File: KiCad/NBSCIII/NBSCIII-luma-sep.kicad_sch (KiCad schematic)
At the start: 11 parts, among them U1 LM324N

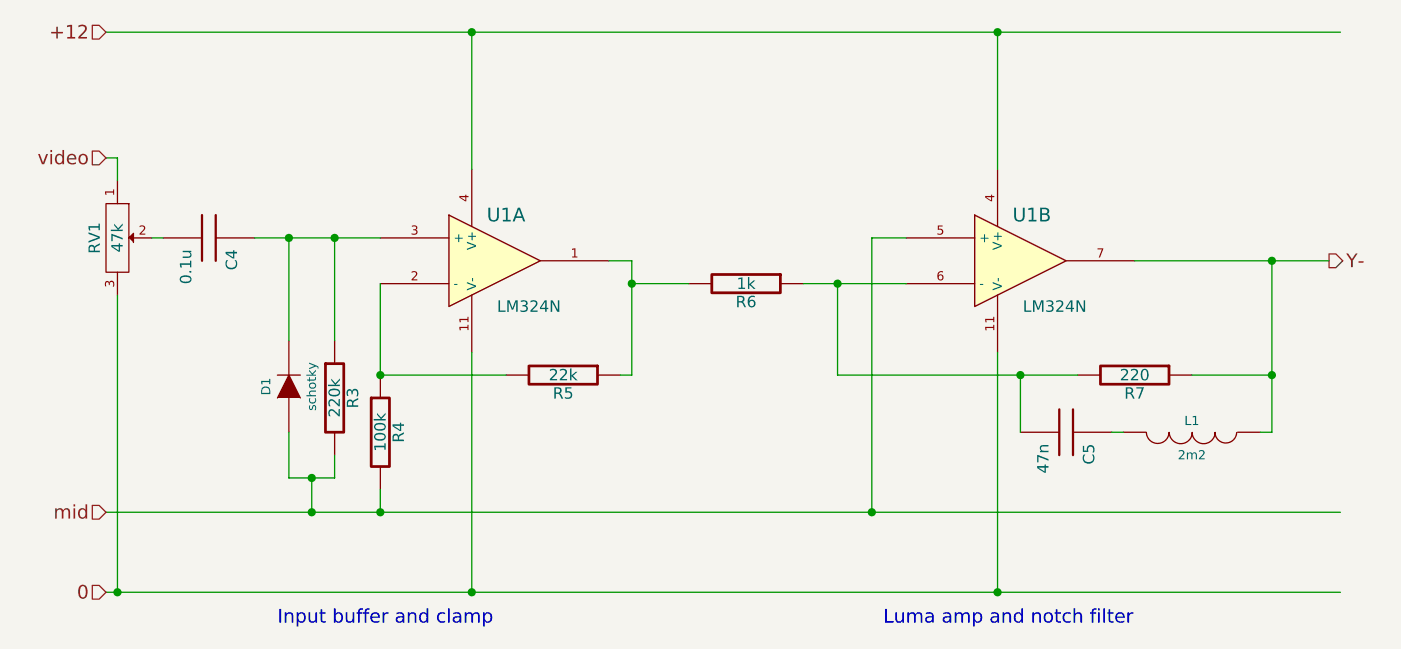
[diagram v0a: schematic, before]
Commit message: unrescue to Device:C
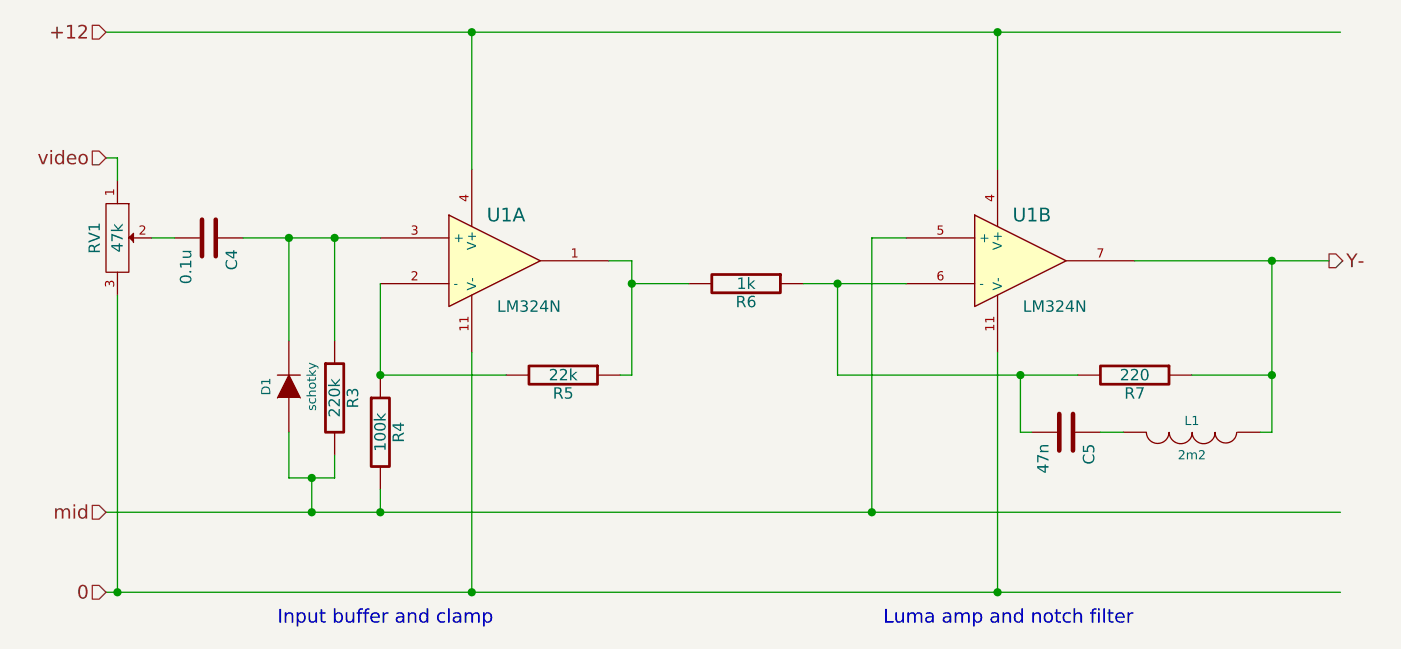
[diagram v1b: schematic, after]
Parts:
- C4, C5: symbol NBSCIII-rescue:C -> Device:C
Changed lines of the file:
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@@
     (stroke (width 0) (type default) (color 0 0 0 0))
   )
-  (wire (pts (xy 48.26 59.69) (xy 49.53 59.69))
+  (wire (pts (xy 48.26 59.69) (xy 50.8 59.69))
     (stroke (width 0) (type default) (color 0 0 0 0))
   )
@@
     (stroke (width 0) (type default) (color 0 0 0 0))
   )
-  (wire (pts (xy 154.94 81.28) (xy 156.21 81.28))
-    (stroke (width 0) (type default) (color 0 0 0 0))
-  )
   (wire (pts (xy 101.6 64.77) (xy 101.6 74.93))
     (stroke (width 0) (type default) (color 0 0 0 0))
@@
     (stroke (width 0) (type default) (color 0 0 0 0))
   )
-  (wire (pts (xy 59.69 59.69) (xy 63.5 59.69))
+  (wire (pts (xy 58.42 59.69) (xy 63.5 59.69))
     (stroke (width 0) (type default) (color 0 0 0 0))
   )
@@
     (stroke (width 0) (type default) (color 0 0 0 0))
   )
+  (wire (pts (xy 144.78 81.28) (xy 146.05 81.28))
+    (stroke (width 0) (type default) (color 0 0 0 0))
+  )
   (wire (pts (xy 66.04 86.36) (xy 63.5 86.36))
     (stroke (width 0) (type default) (color 0 0 0 0))
@@
   )
   (wire (pts (xy 68.58 86.36) (xy 66.04 86.36))
+    (stroke (width 0) (type default) (color 0 0 0 0))
+  )
+  (wire (pts (xy 153.67 81.28) (xy 156.21 81.28))
     (stroke (width 0) (type default) (color 0 0 0 0))
   )
@@
     (pin "3")
   )
-  (symbol (lib_id "NBSCIII-rescue:C") (at 54.61 59.69 270) (unit 1)
+  (symbol (lib_id "Device:C") (at 54.61 59.69 270) (unit 1)
     (in_bom yes) (on_board yes)
     (property "Reference" "C4" (id 0) (at 57.15 60.96 0)
@@
     (pin "2")
   )
-  (symbol (lib_id "NBSCIII-rescue:C") (at 149.86 81.28 270) (unit 1)
+  (symbol (lib_id "Device:C") (at 149.86 81.28 270) (unit 1)
     (in_bom yes) (on_board yes)
     (property "Reference" "C5" (id 0) (at 152.4 82.55 0)

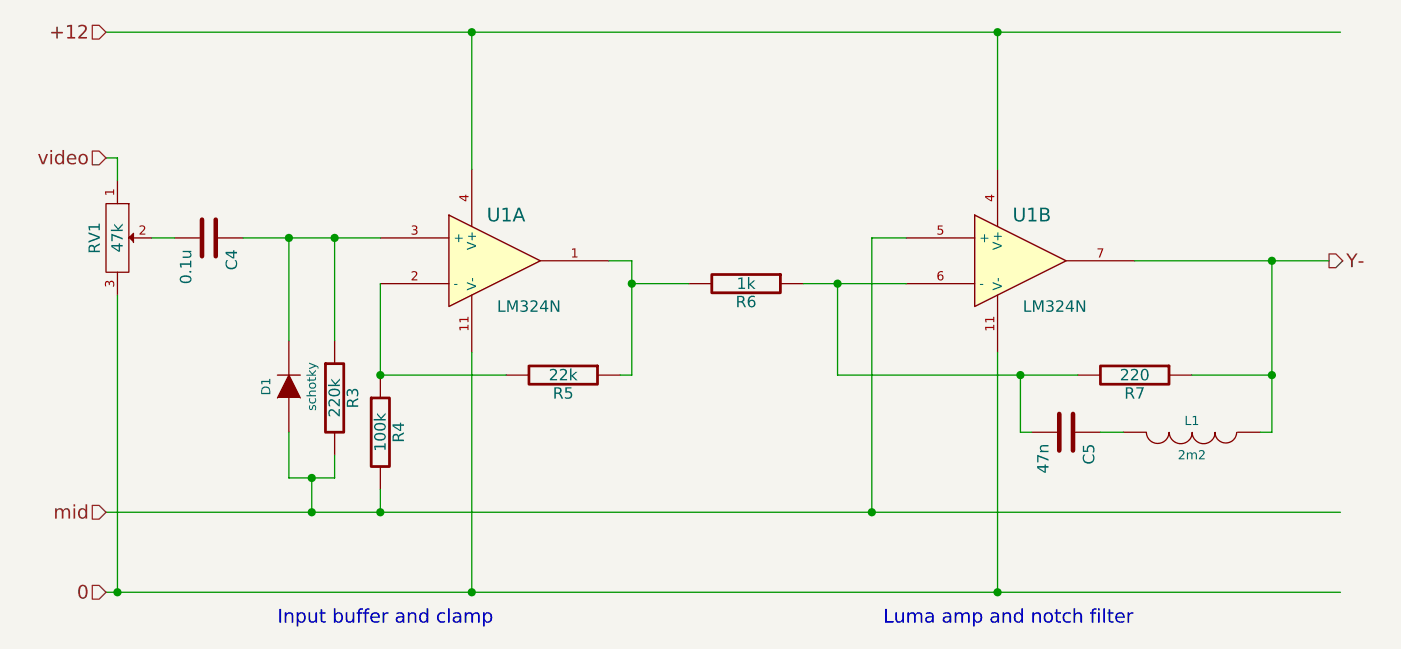
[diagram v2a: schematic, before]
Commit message: unrescue Device:R
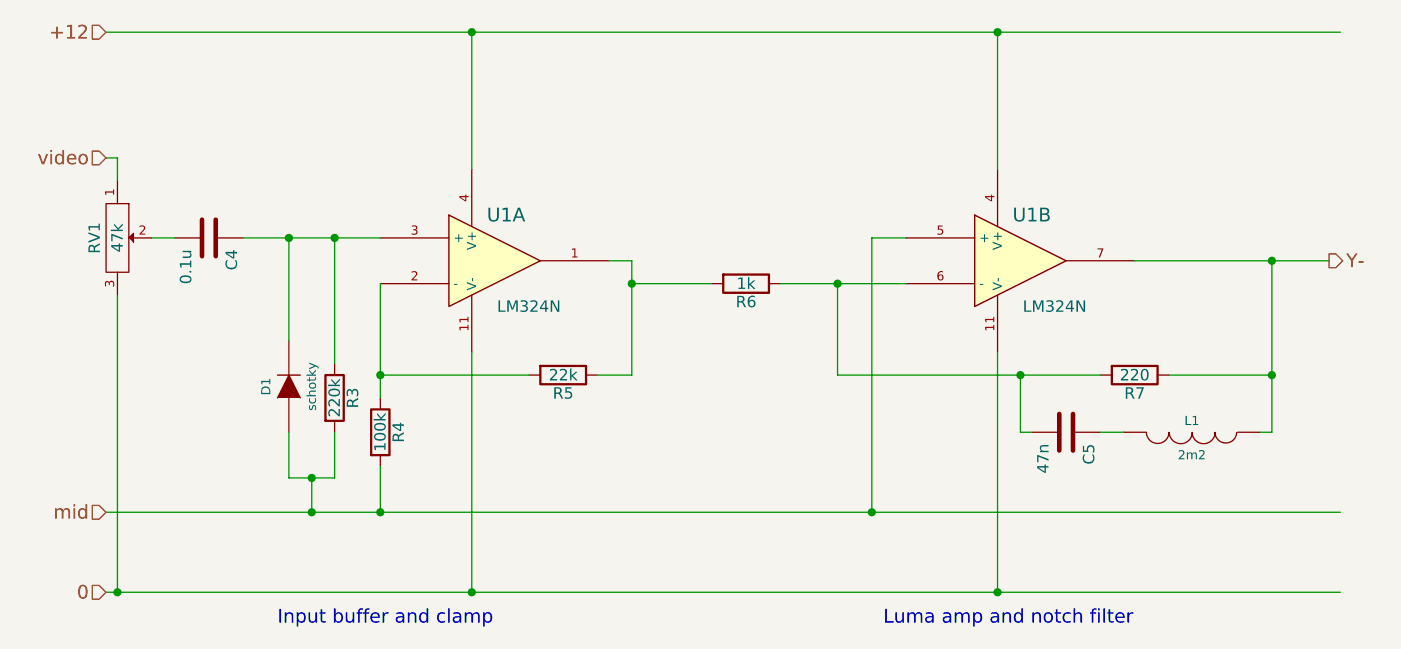
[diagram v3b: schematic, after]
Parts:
- R3, R4, R5, R6, R7: symbol NBSCIII-rescue:R -> Device:R
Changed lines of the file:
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@@
   (junction (at 73.66 90.17) (diameter 0) (color 0 0 0 0)
   )
+  (junction (at 73.66 74.93) (diameter 0) (color 0 0 0 0)
+  )
   (junction (at 172.72 74.93) (diameter 0) (color 0 0 0 0)
   )
@@
   (junction (at 101.6 64.77) (diameter 0) (color 0 0 0 0)
   )
-  (junction (at 73.66 74.93) (diameter 0) (color 0 0 0 0)
-  )
   (junction (at 66.04 86.36) (diameter 0) (color 0 0 0 0)
   )
@@
     (stroke (width 0) (type default) (color 0 0 0 0))
   )
-  (wire (pts (xy 73.66 90.17) (xy 73.66 87.63))
-    (stroke (width 0) (type default) (color 0 0 0 0))
-  )
-  (wire (pts (xy 68.58 59.69) (xy 68.58 71.12))
+  (wire (pts (xy 73.66 85.09) (xy 73.66 90.17))
     (stroke (width 0) (type default) (color 0 0 0 0))
   )
@@
     (stroke (width 0) (type default) (color 0 0 0 0))
   )
+  (wire (pts (xy 68.58 59.69) (xy 68.58 73.66))
+    (stroke (width 0) (type default) (color 0 0 0 0))
+  )
   (wire (pts (xy 73.66 64.77) (xy 73.66 74.93))
     (stroke (width 0) (type default) (color 0 0 0 0))
   )
-  (wire (pts (xy 101.6 64.77) (xy 107.95 64.77))
+  (wire (pts (xy 101.6 64.77) (xy 110.49 64.77))
     (stroke (width 0) (type default) (color 0 0 0 0))
   )
@@
     (stroke (width 0) (type default) (color 0 0 0 0))
   )
+  (wire (pts (xy 73.66 74.93) (xy 73.66 77.47))
+    (stroke (width 0) (type default) (color 0 0 0 0))
+  )
   (wire (pts (xy 63.5 71.12) (xy 63.5 59.69))
     (stroke (width 0) (type default) (color 0 0 0 0))
   )
-  (wire (pts (xy 124.46 64.77) (xy 120.65 64.77))
+  (wire (pts (xy 118.11 64.77) (xy 124.46 64.77))
     (stroke (width 0) (type default) (color 0 0 0 0))
   )
@@
     (stroke (width 0) (type default) (color 0 0 0 0))
   )
-  (wire (pts (xy 73.66 74.93) (xy 87.63 74.93))
+  (wire (pts (xy 73.66 74.93) (xy 90.17 74.93))
     (stroke (width 0) (type default) (color 0 0 0 0))
   )
@@
     (stroke (width 0) (type default) (color 0 0 0 0))
   )
-  (wire (pts (xy 151.13 74.93) (xy 144.78 74.93))
+  (wire (pts (xy 144.78 74.93) (xy 153.67 74.93))
     (stroke (width 0) (type default) (color 0 0 0 0))
   )
@@
     (stroke (width 0) (type default) (color 0 0 0 0))
   )
-  (wire (pts (xy 172.72 74.93) (xy 163.83 74.93))
+  (wire (pts (xy 161.29 74.93) (xy 172.72 74.93))
     (stroke (width 0) (type default) (color 0 0 0 0))
   )
@@
     (stroke (width 0) (type default) (color 0 0 0 0))
   )
-  (wire (pts (xy 68.58 83.82) (xy 68.58 86.36))
+  (wire (pts (xy 68.58 81.28) (xy 68.58 86.36))
     (stroke (width 0) (type default) (color 0 0 0 0))
   )
@@
     (stroke (width 0) (type default) (color 0 0 0 0))
   )
-  (wire (pts (xy 101.6 74.93) (xy 100.33 74.93))
+  (wire (pts (xy 97.79 74.93) (xy 101.6 74.93))
     (stroke (width 0) (type default) (color 0 0 0 0))
   )
@@
     (pin "2")
   )
-  (symbol (lib_id "NBSCIII-rescue:R") (at 68.58 77.47 0) (unit 1)
+  (symbol (lib_id "Device:R") (at 68.58 77.47 0) (unit 1)
     (in_bom yes) (on_board yes)
     (property "Reference" "R3" (id 0) (at 70.612 77.47 90))
@@
     (pin "2")
   )
-  (symbol (lib_id "NBSCIII-rescue:R") (at 73.66 81.28 0) (unit 1)
+  (symbol (lib_id "Device:R") (at 73.66 81.28 0) (unit 1)
     (in_bom yes) (on_board yes)
     (property "Reference" "R4" (id 0) (at 75.692 81.28 90))
@@
     (pin "2")
   )
-  (symbol (lib_id "NBSCIII-rescue:R") (at 93.98 74.93 270) (unit 1)
+  (symbol (lib_id "Device:R") (at 93.98 74.93 270) (unit 1)
     (in_bom yes) (on_board yes)
     (property "Reference" "R5" (id 0) (at 93.98 76.962 90))
@@
     (pin "14")
   )
-  (symbol (lib_id "NBSCIII-rescue:R") (at 114.3 64.77 270) (unit 1)
+  (symbol (lib_id "Device:R") (at 114.3 64.77 270) (unit 1)
     (in_bom yes) (on_board yes)
     (property "Reference" "R6" (id 0) (at 114.3 66.802 90))
@@
     (pin "2")
   )
-  (symbol (lib_id "NBSCIII-rescue:R") (at 157.48 74.93 270) (unit 1)
+  (symbol (lib_id "Device:R") (at 157.48 74.93 270) (unit 1)
     (in_bom yes) (on_board yes)
     (property "Reference" "R7" (id 0) (at 157.48 76.962 90))

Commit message: unrescue Device:R_potentiometer
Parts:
- RV1: symbol NBSCIII-rescue:POT -> Device:R_Potentiometer
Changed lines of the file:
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@@
     (stroke (width 0) (type default) (color 0 0 0 0))
   )
-  (wire (pts (xy 44.45 99.06) (xy 44.45 66.04))
+  (wire (pts (xy 44.45 63.5) (xy 44.45 99.06))
     (stroke (width 0) (type default) (color 0 0 0 0))
   )
@@
   )
   (wire (pts (xy 83.82 52.07) (xy 83.82 36.83))
+    (stroke (width 0) (type default) (color 0 0 0 0))
+  )
+  (wire (pts (xy 44.45 50.8) (xy 44.45 55.88))
     (stroke (width 0) (type default) (color 0 0 0 0))
   )
@@
   )
   (wire (pts (xy 172.72 62.23) (xy 179.07 62.23))
-    (stroke (width 0) (type default) (color 0 0 0 0))
-  )
-  (wire (pts (xy 44.45 53.34) (xy 44.45 50.8))
     (stroke (width 0) (type default) (color 0 0 0 0))
   )
@@
     (pin "14")
   )
-  (symbol (lib_id "NBSCIII-rescue:POT") (at 44.45 59.69 270) (unit 1)
+  (symbol (lib_id "Device:R_Potentiometer") (at 44.45 59.69 0) (unit 1)
     (in_bom yes) (on_board yes)
-    (property "Reference" "RV1" (id 0) (at 41.91 59.69 0))
-    (property "Value" "47k" (id 1) (at 44.45 59.69 0))
+    (property "Reference" "RV1" (id 0) (at 39.37 63.5 0))
+    (property "Value" "47k" (id 1) (at 44.45 59.69 90))
     (property "Footprint" "" (id 2) (at 44.45 59.69 0)
       (effects (font (size 1.27 1.27)) hide)

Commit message: unrescue Device:D
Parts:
- D1: symbol NBSCIII-rescue:DIODE -> Device:D
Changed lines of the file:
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@@
     (stroke (width 0) (type default) (color 0 0 0 0))
   )
-  (wire (pts (xy 63.5 71.12) (xy 63.5 59.69))
+  (wire (pts (xy 63.5 59.69) (xy 63.5 72.39))
     (stroke (width 0) (type default) (color 0 0 0 0))
   )
@@
     (stroke (width 0) (type default) (color 0 0 0 0))
   )
-  (wire (pts (xy 63.5 86.36) (xy 63.5 81.28))
+  (wire (pts (xy 63.5 80.01) (xy 63.5 86.36))
     (stroke (width 0) (type default) (color 0 0 0 0))
   )
@@
     (pin "2")
   )
-  (symbol (lib_id "NBSCIII-rescue:DIODE") (at 63.5 76.2 90) (unit 1)
+  (symbol (lib_id "Device:D") (at 63.5 76.2 90) (unit 1)
     (in_bom yes) (on_board yes)
     (property "Reference" "D1" (id 0) (at 60.96 76.2 0)

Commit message: unrescue Device:L_small
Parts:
- L1: symbol NBSCIII-rescue:INDUCTOR -> Device:L_Small
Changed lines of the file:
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@@
     (stroke (width 0) (type default) (color 0 0 0 0))
   )
-  (wire (pts (xy 153.67 81.28) (xy 156.21 81.28))
+  (wire (pts (xy 153.67 81.28) (xy 161.29 81.28))
     (stroke (width 0) (type default) (color 0 0 0 0))
   )
@@
     (stroke (width 0) (type default) (color 0 0 0 0))
   )
-  (wire (pts (xy 171.45 81.28) (xy 172.72 81.28))
+  (wire (pts (xy 166.37 81.28) (xy 172.72 81.28))
     (stroke (width 0) (type default) (color 0 0 0 0))
   )
@@
     (pin "2")
   )
-  (symbol (lib_id "NBSCIII-rescue:INDUCTOR") (at 163.83 81.28 270) (unit 1)
+  (symbol (lib_id "Device:L_Small") (at 163.83 81.28 270) (unit 1)
     (in_bom yes) (on_board yes)
     (property "Reference" "L1" (id 0) (at 163.83 80.01 90)

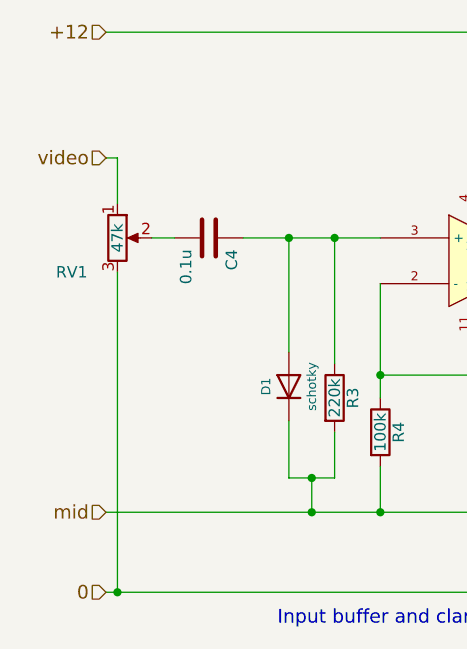
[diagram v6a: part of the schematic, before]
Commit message: Simplify power distribution and make global
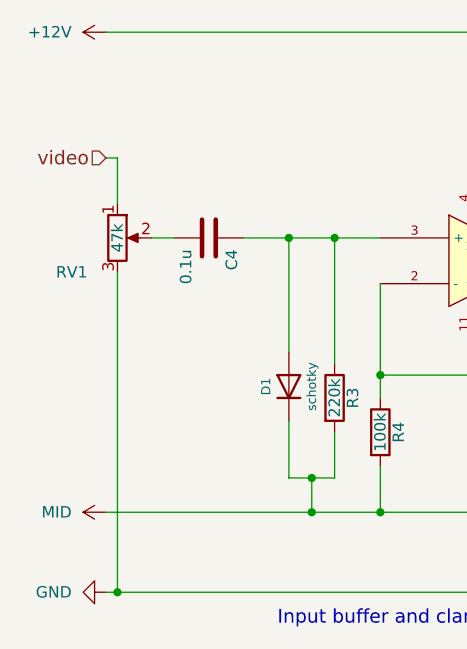
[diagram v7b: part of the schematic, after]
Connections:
- net +12 renamed +12V
- net 0 renamed GND
- net mid renamed MID
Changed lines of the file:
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@@
-    (effects (font (size 1.524 1.524)) (justify right))
-  )
-  (hierarchical_label "+12" (shape input) (at 43.18 36.83 180)
-    (effects (font (size 1.524 1.524)) (justify right))
-  )
-  (hierarchical_label "0" (shape input) (at 43.18 99.06 180)
-    (effects (font (size 1.524 1.524)) (justify right))
-  )
-  (hierarchical_label "mid" (shape input) (at 43.18 90.17 180)
     (effects (font (size 1.524 1.524)) (justify right))
   )
@@
     (pin "2")
   )
+  (symbol (lib_id "NBSCIII:MID") (at 43.18 90.17 90) (unit 1)
+    (in_bom yes) (on_board yes) (fields_autoplaced)
+    (property "Reference" "#PWR0105" (id 0) (at 46.99 90.17 0)
+      (effects (font (size 1.27 1.27)) hide)
+    )
+    (property "Value" "MID" (id 1) (at 39.37 90.1699 90)
+      (effects (font (size 1.27 1.27)) (justify left))
+    )
+    (property "Footprint" "" (id 2) (at 43.18 90.17 0)
+      (effects (font (size 1.27 1.27)) hide)
+    )
+    (property "Datasheet" "" (id 3) (at 43.18 90.17 0)
+      (effects (font (size 1.27 1.27)) hide)
+    )
+    (pin "1")
+  )
+  (symbol (lib_id "power:+12V") (at 43.18 36.83 90) (unit 1)
+    (in_bom yes) (on_board yes) (fields_autoplaced)
+    (property "Reference" "#PWR0104" (id 0) (at 46.99 36.83 0)
+      (effects (font (size 1.27 1.27)) hide)
+    )
+    (property "Value" "+12V" (id 1) (at 39.37 36.8299 90)
+      (effects (font (size 1.27 1.27)) (justify left))
+    )
+    (property "Footprint" "" (id 2) (at 43.18 36.83 0)
+      (effects (font (size 1.27 1.27)) hide)
+    )
+    (property "Datasheet" "" (id 3) (at 43.18 36.83 0)
+      (effects (font (size 1.27 1.27)) hide)
+    )
+    (pin "1")
+  )
+  (symbol (lib_id "power:GND") (at 43.18 99.06 270) (unit 1)
+    (in_bom yes) (on_board yes) (fields_autoplaced)
+    (property "Reference" "#PWR0106" (id 0) (at 36.83 99.06 0)
+      (effects (font (size 1.27 1.27)) hide)
+    )
+    (property "Value" "GND" (id 1) (at 39.37 99.0599 90)
+      (effects (font (size 1.27 1.27)) (justify right))
+    )
+    (property "Footprint" "" (id 2) (at 43.18 99.06 0)
+      (effects (font (size 1.27 1.27)) hide)
+    )
+    (property "Datasheet" "" (id 3) (at 43.18 99.06 0)
+      (effects (font (size 1.27 1.27)) hide)
+    )
+    (pin "1")
+  )
 )
